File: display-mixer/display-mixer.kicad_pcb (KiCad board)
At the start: 2 copper layers, 67.6 x 67 mm, 9 parts, among them J1 Conn_01x42, U1 ER-TFT062, U2 LS021B7DD02

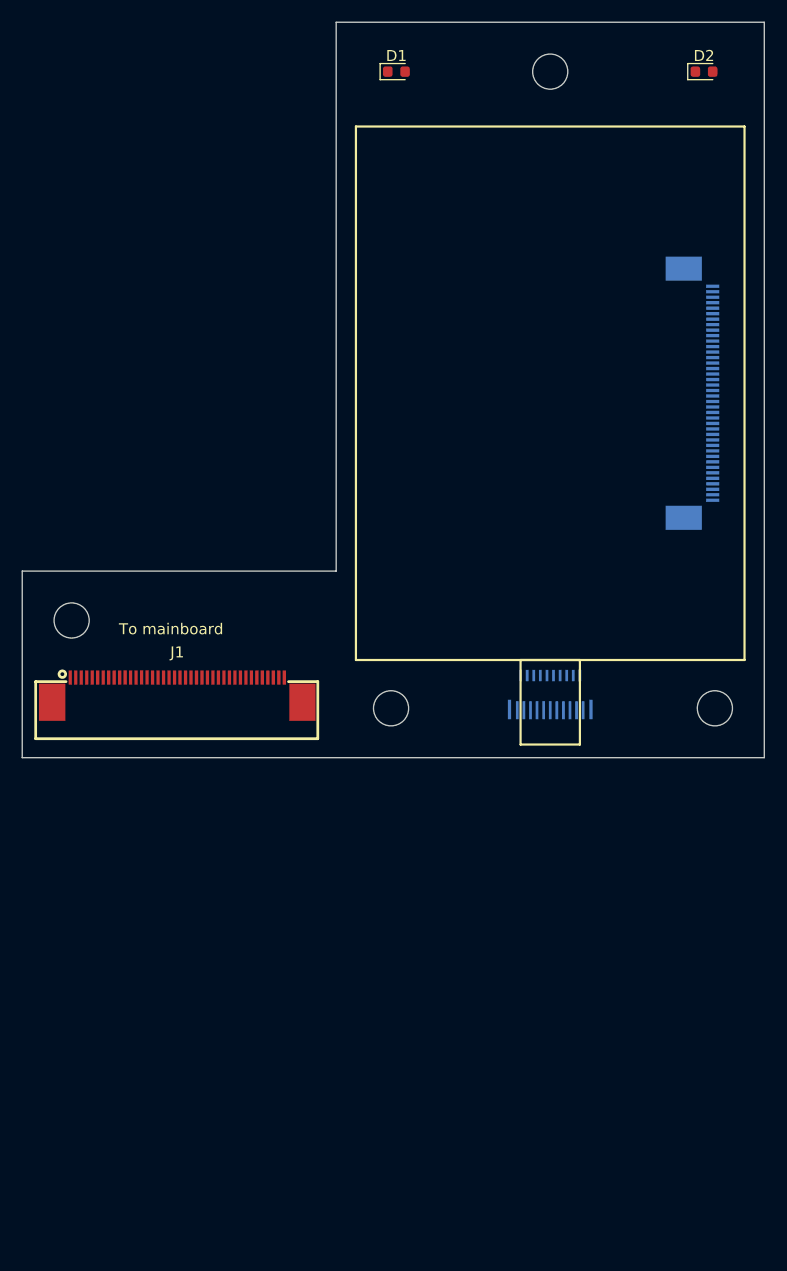
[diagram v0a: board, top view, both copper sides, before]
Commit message: Move main connector on display mixer and consolidate keyboard to single sheet.
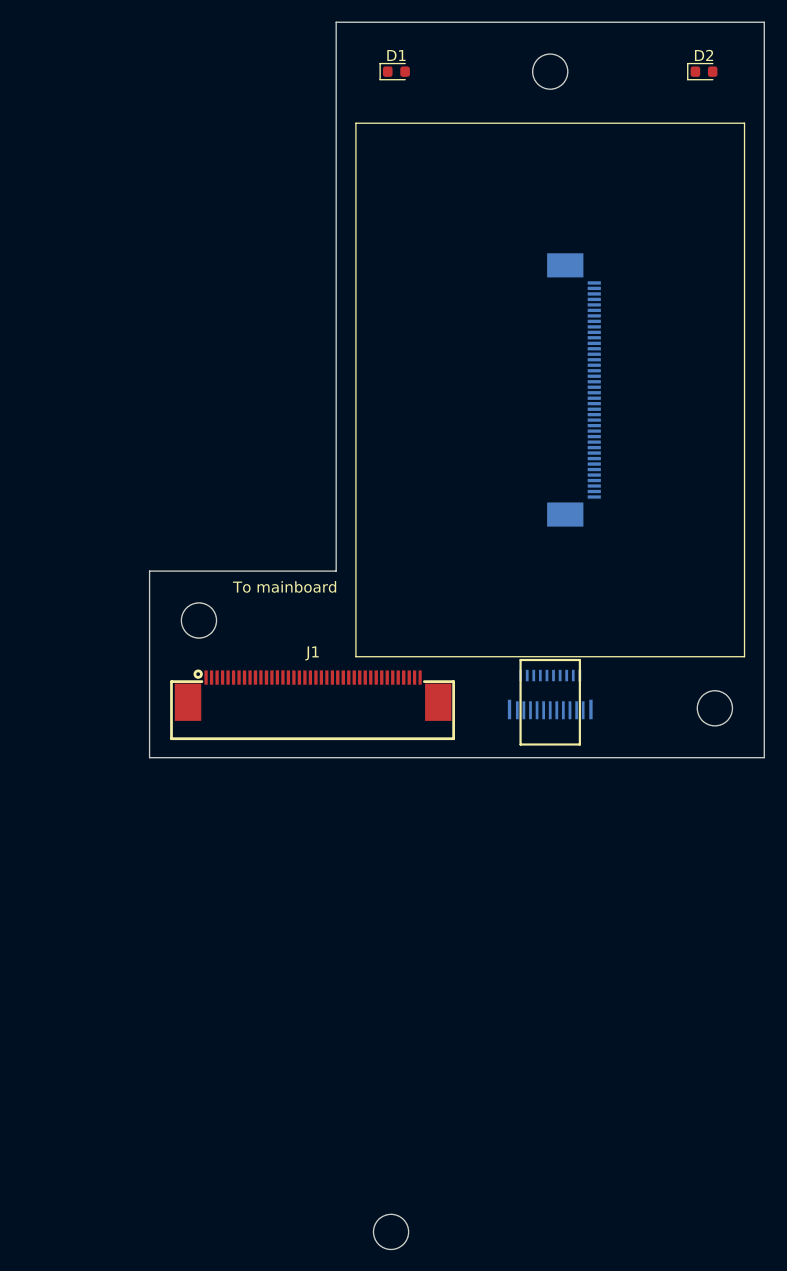
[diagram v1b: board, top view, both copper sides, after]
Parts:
- moved H2 47.7 mm to (109.0, 139.8)
- moved J1 12.4 mm to (102.0, 90.4)
- moved H4 11.6 mm to (91.5, 84.1)
- moved U1 10.8 mm to (126.2, 63.1)
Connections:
- U1 pad 5: unconnected-(U1-VDD-Pad5) -> +3V3
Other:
- board size 67.6 x 67 mm -> 56 x 67 mm
- board text added: "2mm"
- board text added: "56mm"
- board text removed: "29.5mm"
- board text removed: "33.6mm"
- board text removed: "68mm"
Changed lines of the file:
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@@
 	(footprint "kirdos:JUSHUO_AFC07-S40FCC-00-FPC-SMD-0.5P"
 		(layer "F.Cu")
-		(at 89.575 90.395)
+		(at 101.95 90.395)
 		(descr "FPC 0.5mm 40P H2.0mm")
 		(property "Reference" "J1"
@@
 	(footprint "MountingHole:MountingHole_3.2mm_M3"
 		(layer "F.Cu")
-		(at 79.95 84.075)
+		(at 91.55 84.075)
 		(descr "Mounting Hole 3.2mm, M3, no annular, generated by kicad-footprint-generator mountinghole.py")
 		(tags "mountinghole M3")
@@
 	(footprint "MountingHole:MountingHole_3.2mm_M3"
 		(layer "F.Cu")
-		(at 109.05 92.075)
+		(at 109.05 139.775)
 		(descr "Mounting Hole 3.2mm, M3, no annular, generated by kicad-footprint-generator mountinghole.py")
 		(tags "mountinghole M3")
@@
 			)
 		)
-		(attr through_hole)
+		(attr smd)
 		(duplicate_pad_numbers_are_jumpers no)
 		(fp_line
@@
 	(footprint "kirdos:JUSHUO_AFC07-S40ECA-00-FPC-SMD_P0.50-40P_LCS-SJ-H2.0"
 		(layer "B.Cu")
-		(at 137.03 63.375 -90)
+		(at 126.2425 63.075 -90)
 		(property "Reference" "U1"
 			(at 0 5.318 90)
@@
 			(size 0.3 1.2)
 			(layers "B.Cu" "B.Mask" "B.Paste")
-			(net "unconnected-(U1-VDD-Pad5)")
+			(net "+3V3")
 			(pinfunction "VDD_5")
 			(pintype "power_in")
@@
 	)
 	(gr_rect
-		(start 105.85 39.075)
-		(end 141.25 87.675)
+		(start 105.85 38.775)
+		(end 141.25 87.375)
 		(stroke
-			(width 0.2)
-			(type solid)
+			(width 0.1)
+			(type default)
 		)
 		(fill no)
@@
 	)
 	(gr_rect
-		(start 105.85 39.075)
-		(end 141.25 87.675)
+		(start 105.85 38.775)
+		(end 141.25 87.375)
 		(stroke
 			(width 0.1)
@@
 	)
 	(gr_line
-		(start 74 79.575)
-		(end 74 96.575)
+		(start 85.5 79.575)
+		(end 85.5 96.575)
 		(stroke
 			(width 0.1)
@@
 	)
 	(gr_line
-		(start 75.45 97.575)
-		(end 143.45 97.575)
+		(start 87.05 97.575)
+		(end 143.075 97.575)
 		(stroke
 			(width 0.1)
@@
 	)
 	(gr_line
-		(start 79.95 84.075)
-		(end 79.95 96.575)
+		(start 89.05 94.845)
+		(end 87.05 94.845)
+		(stroke
+			(width 0.1)
+			(type solid)
+		)
+		(layer "Cmts.User")
+	)
+	(gr_line
+		(start 91.45 84.075)
+		(end 91.45 96.575)
 		(stroke
 			(width 0.1)
@@
 	)
 	(gr_line
-		(start 109.05 92.075)
-		(end 75.45 92.075)
-		(stroke
-			(width 0.1)
-			(type default)
-		)
-		(layer "Cmts.User")
-	)
-	(gr_line
 		(start 123.55 34.075)
 		(end 101.95 34.075)
@@
 	)
 	(gr_line
-		(start 138.55 92.075)
-		(end 109.05 92.075)
-		(stroke
-			(width 0.1)
-			(type solid)
-		)
-		(layer "Cmts.User")
-	)
-	(gr_line
 		(start 141.25 87.675)
 		(end 143.05 87.675)
@@
 	(gr_poly
 		(pts
-			(xy 143.05 96.575) (xy 143.05 29.575) (xy 104.05 29.575) (xy 104.05 79.575) (xy 75.45 79.575) (xy 75.45 96.575)
+			(xy 143.05 96.575) (xy 143.05 29.575) (xy 104.05 29.575) (xy 104.05 79.575) (xy 87.05 79.575) (xy 87.05 96.575)
 		)
 		(stroke
@@
 	)
 	(gr_text "To mainboard"
-		(at 84.257143 85.45 0)
+		(at 94.65 81.65 0)
 		(layer "F.SilkS")
 		(effects
@@
 		)
 	)
-	(gr_text "33.6mm"
-		(at 92.25 92.075 0)
-		(layer "Cmts.User")
-		(effects
-			(font
-				(size 1 1)
-				(thickness 0.15)
-			)
-			(justify left bottom)
-		)
-	)
-	(gr_text "68mm"
-		(at 97.85 99.25 0)
+	(gr_text "2mm"
+		(at 85.275 95.95 0)
 		(layer "Cmts.User")
 		(effects
@@
 		)
 	)
+	(gr_text "56mm"
+		(at 112.475 99.25 0)
+		(layer "Cmts.User")
+		(effects
+			(font
+				(size 1 1)
+				(thickness 0.15)
+			)
+			(justify left bottom)
+		)
+	)
 	(gr_text "39mm"
 		(at 120.875 29.525 0)
@@
 		)
 	)
-	(gr_text "29.5mm"
-		(at 128.2 92 0)
-		(layer "Cmts.User")
-		(effects
-			(font
-				(size 1 1)
-				(thickness 0.15)
-			)
-			(justify left bottom)
-		)
-	)
 	(gr_text "LS021 FFC is 21.02mm. Bottom of\nLS021 here to edge of board is 8.9mm.\nBottom of board to LS021 connector back\nis 5.865mm, so total length needed\nexcluding wrap is 14.765mm."
 		(at 146.775 90.425 0)
@@
 	)
 	(gr_text "17mm"
-		(at 73.525 89.8 90)
+		(at 85.2 89.8 90)
 		(layer "Cmts.User")
 		(effects
@@
 	)
 	(gr_text "12.5mm"
-		(at 79.7 96.575 90)
+		(at 91.2 96.575 90)
 		(layer "Cmts.User")
 		(effects
